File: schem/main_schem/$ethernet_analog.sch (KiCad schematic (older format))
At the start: 11 parts, among them U1 SPDT_ANALOG, U2 SPDT_ANALOG

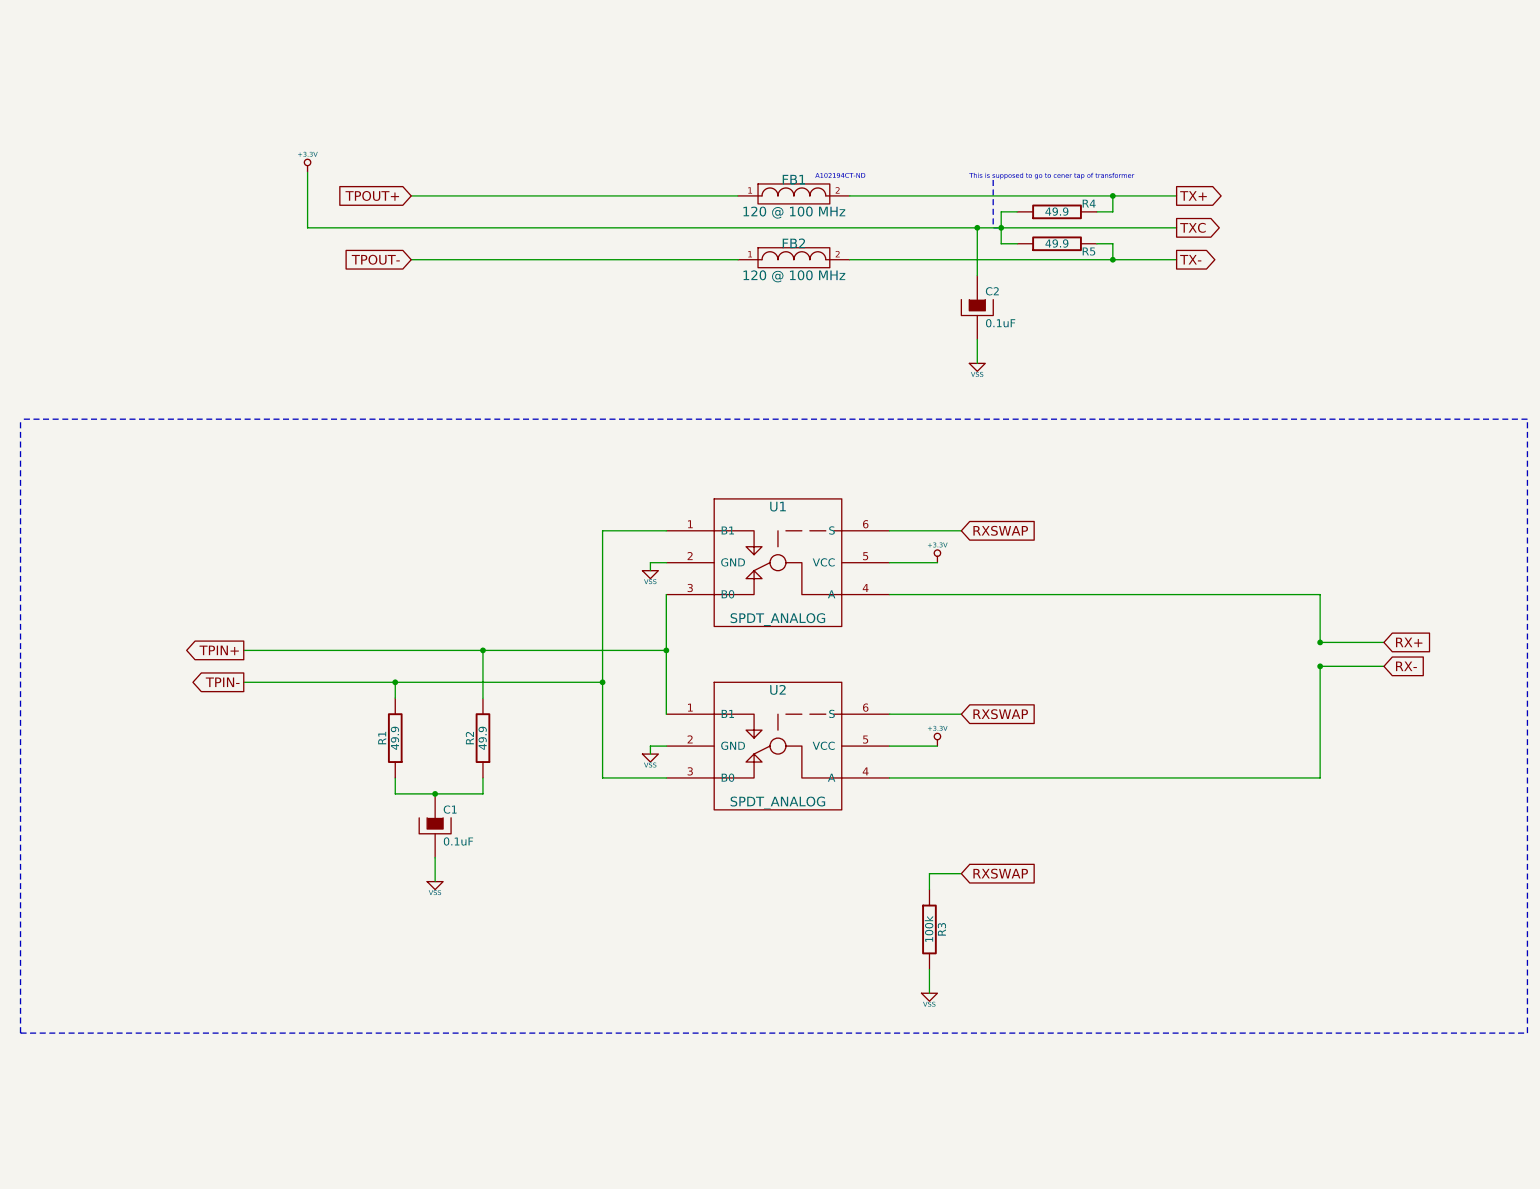
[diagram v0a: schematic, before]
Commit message: Board has own RJ45 jack, finish nearly all logic of board, add QELink screenprint
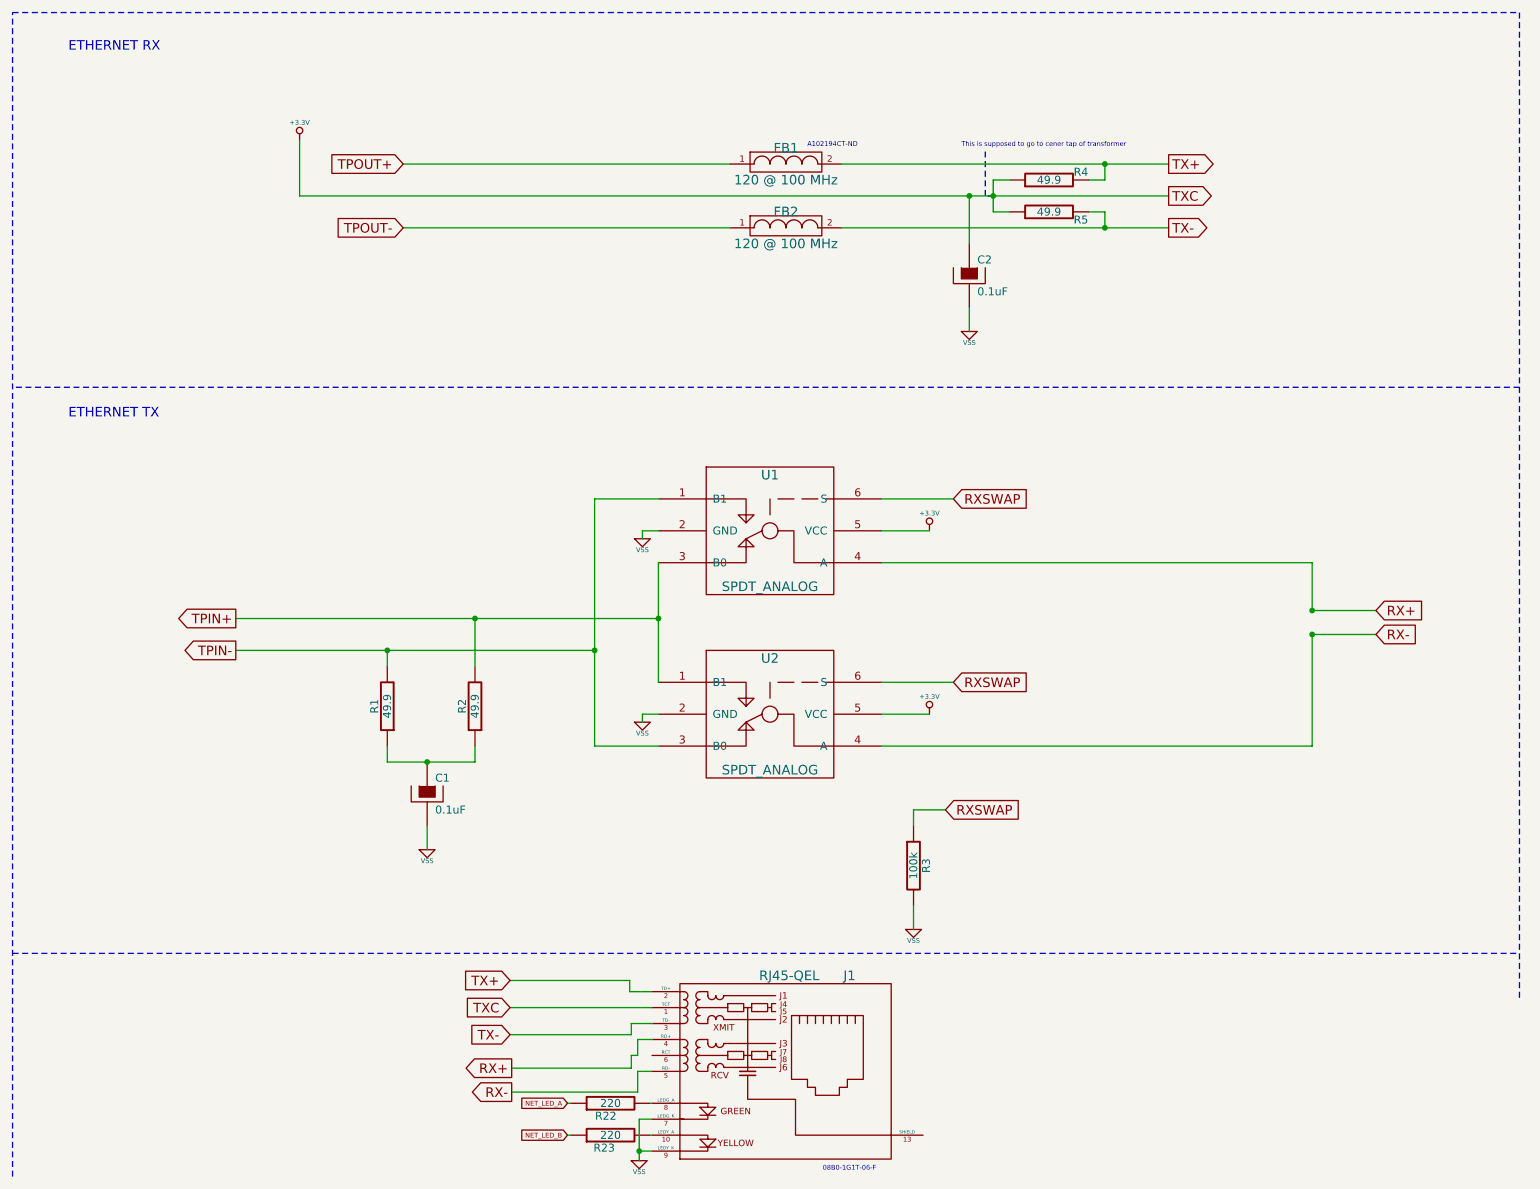
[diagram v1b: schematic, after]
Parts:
- added J1: RJ45-QEL, symbol RJ45-QEL
- added R22, R23: 220, symbol R
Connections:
- net +3.3V: now also J1.1 (TCT)
- net RX+: now also J1.4 (RD+)
- net RX-: now also J1.5 (RD-)
- net TX+: now also J1.2 (TD+)
- net TX-: now also J1.3 (TD-)
- net VSS: now also J1.7 (LEDG_K), J1.9 (LEDY_K)
- new net: J1.10 (LEDY_A), R23.2
- new net: J1.8 (LEDG_A), R22.2
- new net NET_LED_A: R22.1
- new net NET_LED_B: R23.1
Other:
- note added: "08B0-1G1T-06-F"
- note added: "ETHERNET RX"
- note added: "ETHERNET TX"
- moved on the sheet: C1, C2, FB1, FB2, R1, R2, R3, R4, R5, U1, U2
